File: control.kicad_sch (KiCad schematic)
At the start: 22 parts, among them Q1601 SI2369, Q1602 BSS138, Q1603 MMBT3904, Q1604 SI2369, Q1605 BSS138, Q1606 MMBT3904

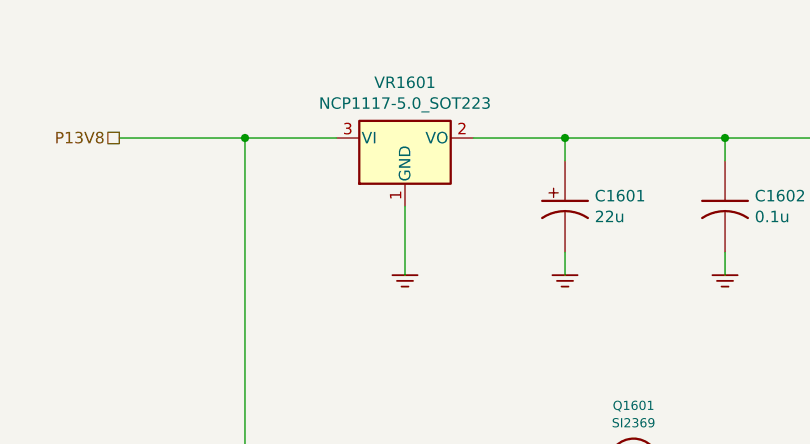
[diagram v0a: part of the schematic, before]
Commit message: Update pcb database to version 6
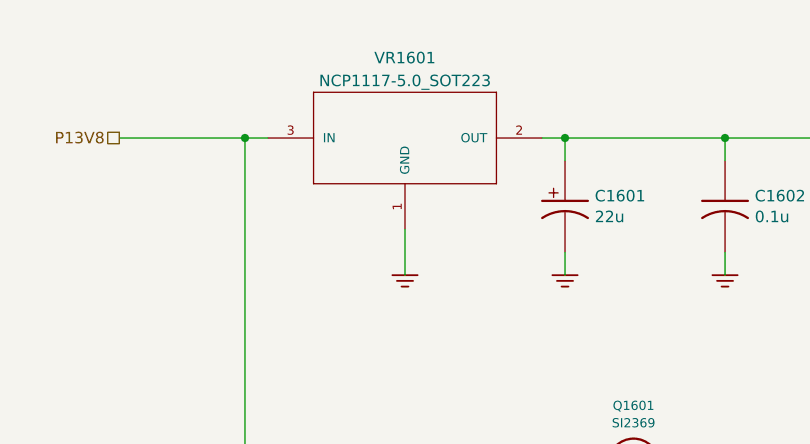
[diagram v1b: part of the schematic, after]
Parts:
- C1601: symbol Custom:CP_US -> custom:CP_US; PartNumber 800267-226 -> 80000X-XXX
- C1602: symbol Custom:C_US_0805_0.1UF_X7R_10%_50V_HS -> custom:C_US_0805_0.1UF_X7R_10%_50V_HS
- C1603: footprint Capacitor_SMD:C_0805_2012Metric_Pad1.15x1.40mm_HandSolder -> Capacitor_SMD:C_0603_1608Metric; symbol Custom:C_US -> custom:C_US; PartNumber 800003-475 -> 800063-XXX
- Q1601, Q1604: footprint mods:SOT23-3-SAR -> SOT-23; symbol Custom:AO3407 -> custom:AO3407
- Q1602, Q1605: footprint mods:SOT23-3-SAR -> SOT-23; symbol Custom:BSS138 -> custom:BSS138
- Q1603, Q1606: symbol Custom:MMBT3904 -> custom:MMBT3904
- R1601: symbol Custom:R_US_0805_1%_HS -> custom:R_US_0805_1%_HS; PartNumber 800235-471 -> 800235-XXX
- R1602, R1605, R1606, R1609: symbol Custom:R_US_0805_1%_HS -> custom:R_US_0805_1%_HS; PartNumber 800235-103 -> 800235-XXX
- R1603, R1607: symbol Custom:R_US_0805_1%_HS -> custom:R_US_0805_1%_HS; PartNumber 800235-100 -> 800235-XXX
- R1604, R1608: symbol Custom:R_US_0805_1%_HS -> custom:R_US_0805_1%_HS; PartNumber 800235-101 -> 800235-XXX
- TP1601, TP1602, TP1603: footprint mods:TESTPIN -> TESTPIN; symbol Custom:TESTPINTPSQ025 -> custom:TESTPINTPSQ025
- VR1601: footprint Package_TO_SOT_SMD:SOT-223-3_TabPin2 -> SOT223; symbol Regulator_Linear:NCP1117-5.0_SOT223 -> custom:NCP1117ST50

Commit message: Sync PCB with schematic
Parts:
- VR1601: footprint SOT223 -> Package_TO_SOT_SMD:SOT-223
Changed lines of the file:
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@@
     (property "Reference" "VR1601" (id 0) (at 64.77 29.21 0))
     (property "Value" "NCP1117-5.0_SOT223" (id 1) (at 64.77 31.75 0))
-    (property "Footprint" "SOT223" (id 2) (at 64.77 34.29 0)
+    (property "Footprint" "Package_TO_SOT_SMD:SOT-223" (id 2) (at 64.77 34.29 0)
       (effects (font (size 1.27 1.27)) hide)
     )

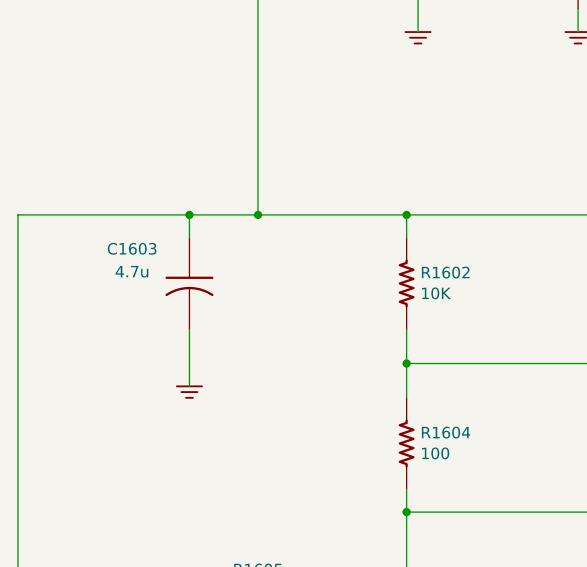
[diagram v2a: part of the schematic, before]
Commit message: Fix BOM part number errors and out of sync footprints which happened during conversion from Kicad 5 to 6
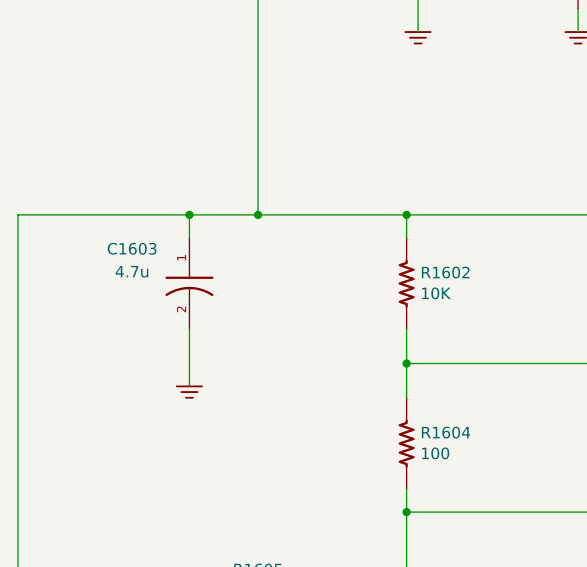
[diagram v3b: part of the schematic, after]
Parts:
- C1601: PartNumber 80000X-XXX -> 800267-226
- C1603: footprint Capacitor_SMD:C_0603_1608Metric -> Capacitor_SMD:C_0805_2012Metric_Pad1.18x1.45mm_HandSolder; PartNumber 800063-XXX -> 800003-475
- Q1602, Q1605: footprint SOT-23 -> mods:SOT23-3-SAR
- R1601: PartNumber 800235-XXX -> 800235-471
- R1602, R1605, R1606, R1609: PartNumber 800235-XXX -> 800235-103
- R1603, R1607: PartNumber 800235-XXX -> 800235-100
- R1604, R1608: PartNumber 800235-XXX -> 800235-101
- VR1601: footprint Package_TO_SOT_SMD:SOT-223 -> Package_TO_SOT_SMD:SOT-223-3_TabPin2
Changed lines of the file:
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@@
       (effects (font (size 1.524 1.524)))
     )
-    (property "PartNumber" "800235-XXX" (id 4) (at 68.072 78.74 90)
+    (property "PartNumber" "800235-103" (id 4) (at 68.072 78.74 90)
       (effects (font (size 1.524 1.524)) hide)
     )
@@
       (effects (font (size 1.524 1.524)))
     )
-    (property "PartNumber" "800235-XXX" (id 4) (at 68.072 96.52 90)
+    (property "PartNumber" "800235-101" (id 4) (at 68.072 96.52 90)
       (effects (font (size 1.524 1.524)) hide)
     )
@@
       (effects (font (size 1.524 1.524)))
     )
-    (property "PartNumber" "800235-XXX" (id 4) (at 49.53 122.682 90)
+    (property "PartNumber" "800235-103" (id 4) (at 49.53 122.682 90)
       (effects (font (size 1.524 1.524)) hide)
     )
@@
       (effects (font (size 1.524 1.524)))
     )
-    (property "PartNumber" "800235-XXX" (id 4) (at 113.792 81.28 90)
+    (property "PartNumber" "800235-100" (id 4) (at 113.792 81.28 90)
       (effects (font (size 1.524 1.524)) hide)
     )
@@
       (effects (font (size 1.016 1.016)) (justify left))
     )
-    (property "Footprint" "SOT-23" (id 2) (at 103.378 102.8192 0)
+    (property "Footprint" "mods:SOT23-3-SAR" (id 2) (at 103.378 102.8192 0)
       (effects (font (size 0.7366 0.7366)) hide)
     )
@@
       (effects (font (size 1.524 1.524)))
     )
-    (property "PartNumber" "800235-XXX" (id 4) (at 68.072 142.24 90)
+    (property "PartNumber" "800235-103" (id 4) (at 68.072 142.24 90)
       (effects (font (size 1.524 1.524)) hide)
     )
@@
       (effects (font (size 1.524 1.524)))
     )
-    (property "PartNumber" "800235-XXX" (id 4) (at 68.072 160.02 90)
+    (property "PartNumber" "800235-101" (id 4) (at 68.072 160.02 90)
       (effects (font (size 1.524 1.524)) hide)
     )
@@
       (effects (font (size 1.524 1.524)))
     )
-    (property "PartNumber" "800235-XXX" (id 4) (at 49.53 186.182 90)
+    (property "PartNumber" "800235-103" (id 4) (at 49.53 186.182 90)
       (effects (font (size 1.524 1.524)) hide)
     )
@@
       (effects (font (size 1.524 1.524)))
     )
-    (property "PartNumber" "800235-XXX" (id 4) (at 113.792 144.78 90)
+    (property "PartNumber" "800235-100" (id 4) (at 113.792 144.78 90)
       (effects (font (size 1.524 1.524)) hide)
     )
@@
       (effects (font (size 1.016 1.016)) (justify left))
     )
-    (property "Footprint" "SOT-23" (id 2) (at 103.378 166.3192 0)
+    (property "Footprint" "mods:SOT23-3-SAR" (id 2) (at 103.378 166.3192 0)
       (effects (font (size 0.7366 0.7366)) hide)
     )
@@
     (property "Reference" "C1603" (id 0) (at 33.02 77.47 0))
     (property "Value" "4.7u" (id 1) (at 33.02 80.01 0))
-    (property "Footprint" "Capacitor_SMD:C_0603_1608Metric" (id 2) (at 41.91 69.85 0)
+    (property "Footprint" "Capacitor_SMD:C_0805_2012Metric_Pad1.18x1.45mm_HandSolder" (id 2) (at 41.91 69.85 0)
       (effects (font (size 1.524 1.524)) hide)
     )
@@
       (effects (font (size 1.524 1.524)))
     )
-    (property "PartNumber" "800063-XXX" (id 4) (at 39.37 67.31 0)
+    (property "PartNumber" "800003-475" (id 4) (at 39.37 67.31 0)
       (effects (font (size 1.524 1.524)) hide)
     )
@@
     (property "Reference" "VR1601" (id 0) (at 64.77 29.21 0))
     (property "Value" "NCP1117-5.0_SOT223" (id 1) (at 64.77 31.75 0))
-    (property "Footprint" "Package_TO_SOT_SMD:SOT-223" (id 2) (at 64.77 34.29 0)
+    (property "Footprint" "Package_TO_SOT_SMD:SOT-223-3_TabPin2" (id 2) (at 64.77 34.29 0)
       (effects (font (size 1.27 1.27)) hide)
     )
@@
       (effects (font (size 1.524 1.524)))
     )
-    (property "PartNumber" "80000X-XXX" (id 4) (at 86.36 40.64 0)
+    (property "PartNumber" "800267-226" (id 4) (at 86.36 40.64 0)
       (effects (font (size 1.524 1.524)) hide)
     )
@@
       (effects (font (size 1.524 1.524)))
     )
-    (property "PartNumber" "800235-XXX" (id 4) (at 126.492 44.45 90)
-      (effects (font (size 1.524 1.524)) hide)
-    )
+    (property "PartNumber" "800235-471" (id 4) (at 126.492 44.45 90)
+      (effects (font (size 1.524 1.524)) hide)
+    )

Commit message: Change bias resistors on 2SC3357 amplifiers to stay under 12V across Vbe.
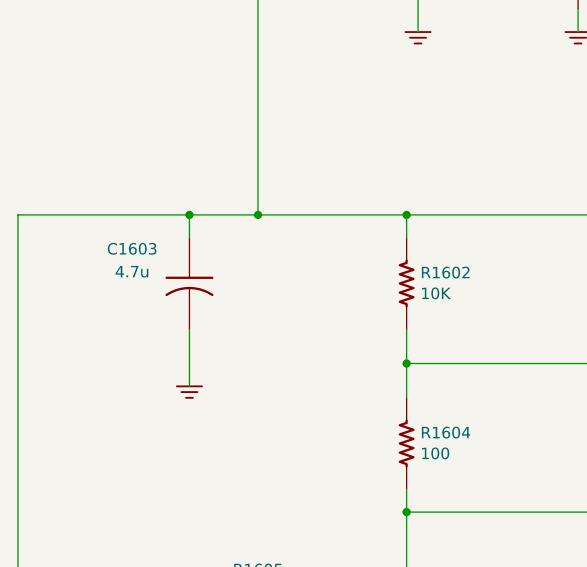
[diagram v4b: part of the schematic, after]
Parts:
- C1603: footprint Capacitor_SMD:C_0805_2012Metric_Pad1.18x1.45mm_HandSolder -> Capacitor_SMD:C_0603_1608Metric; PartNumber 800003-475 -> 800063-XXX
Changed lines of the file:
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@@
     (property "Reference" "C1603" (id 0) (at 33.02 77.47 0))
     (property "Value" "4.7u" (id 1) (at 33.02 80.01 0))
-    (property "Footprint" "Capacitor_SMD:C_0805_2012Metric_Pad1.18x1.45mm_HandSolder" (id 2) (at 41.91 69.85 0)
+    (property "Footprint" "Capacitor_SMD:C_0603_1608Metric" (id 2) (at 41.91 69.85 0)
       (effects (font (size 1.524 1.524)) hide)
     )
@@
       (effects (font (size 1.524 1.524)))
     )
-    (property "PartNumber" "800003-475" (id 4) (at 39.37 67.31 0)
+    (property "PartNumber" "800063-XXX" (id 4) (at 39.37 67.31 0)
       (effects (font (size 1.524 1.524)) hide)
     )

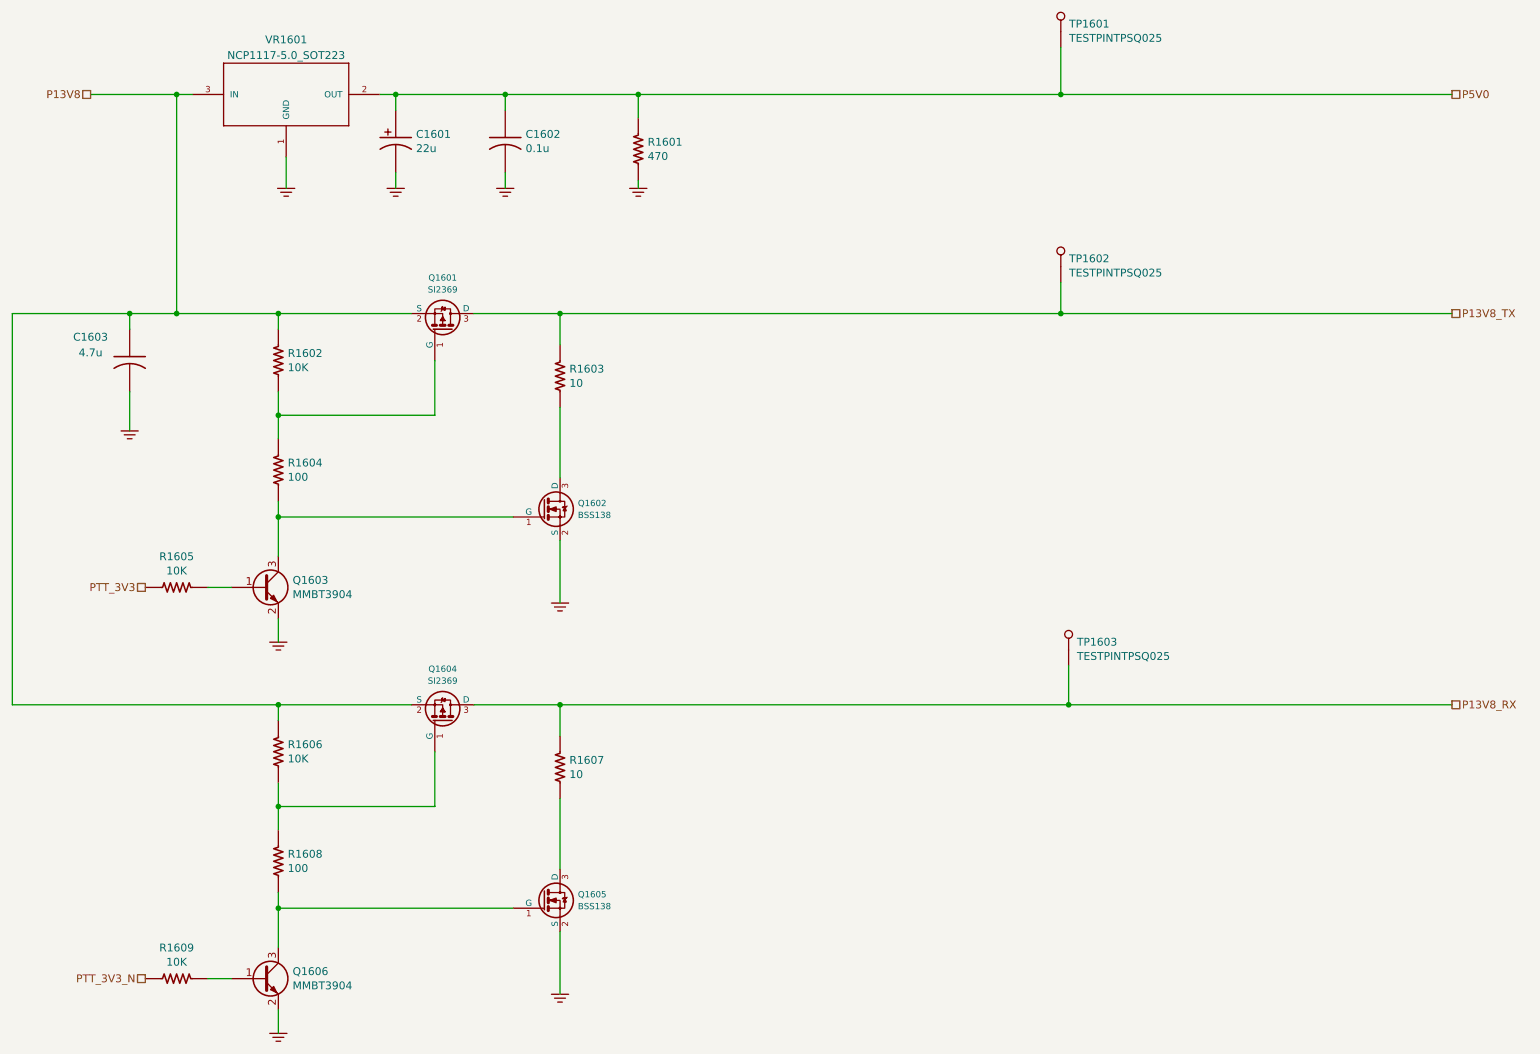
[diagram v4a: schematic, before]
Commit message: trx_mobo_concept_2_B. Change design to use a dedicated 8V supply for the 2SC3357 parts. Add S-Meter connector. Change mic connector to 3 pins and add 8V sopower supply to pin 3.
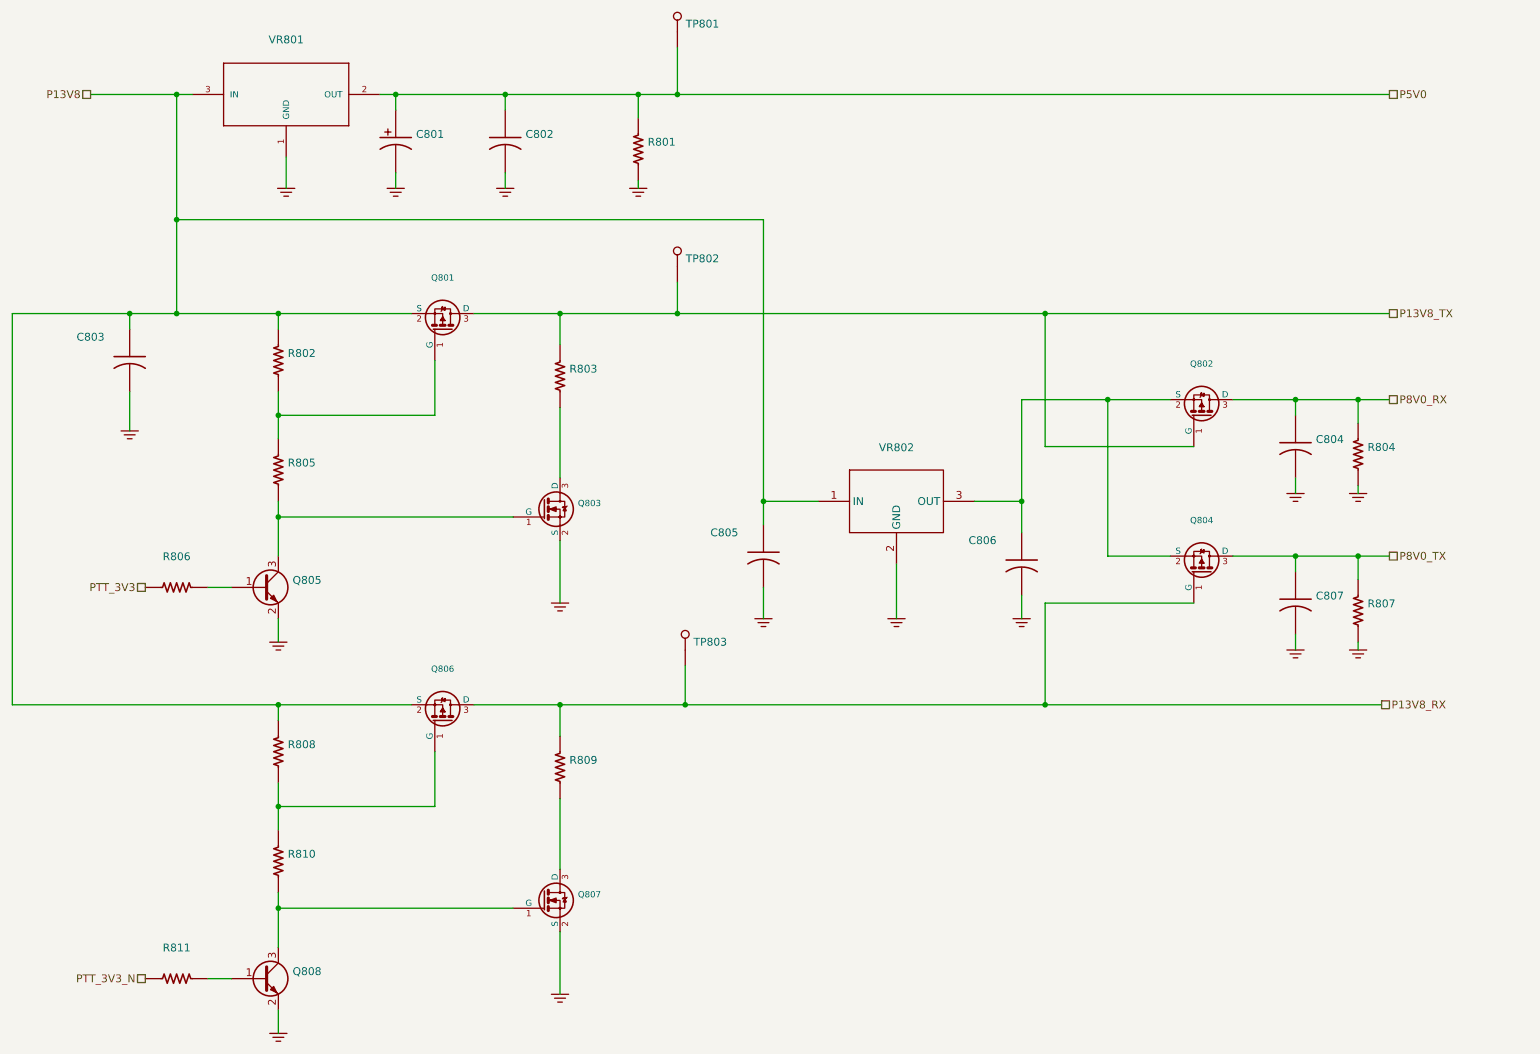
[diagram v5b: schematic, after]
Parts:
- added C804, C807: (no value), symbol custom:C_US_0805_0.1UF_X7R_10%_50V_HS
- added C805, C806: (no value), symbol custom:C_US
- added Q802, Q804: (no value), symbol custom:AO3407
- added R804, R807: (no value), symbol custom:R_US_0805_1%_HS
- added VR802: (no value), symbol custom:MC78M08CDTRKG
- C801: renamed from C1601; value 22u -> (none); footprint Capacitor_SMD:CP_Elec_6.3x5.7 -> (none)
- C802: renamed from C1602; value 0.1u -> (none); footprint Capacitor_SMD:C_0805_2012Metric_Pad1.15x1.40mm_HandSolder -> (none)
- C803: renamed from C1603; value 4.7u -> (none); footprint Capacitor_SMD:C_0603_1608Metric -> (none); PartNumber 800063-XXX -> 800003-475
- Q801: renamed from Q1601; value SI2369 -> (none); footprint SOT-23 -> (none)
- Q803: renamed from Q1602; value BSS138 -> (none); footprint mods:SOT23-3-SAR -> (none)
- Q805: renamed from Q1603; value MMBT3904 -> (none); footprint mods:SOT23-3-SAR -> (none)
- Q806: renamed from Q1604; value SI2369 -> (none); footprint SOT-23 -> (none)
- Q807: renamed from Q1605; value BSS138 -> (none); footprint mods:SOT23-3-SAR -> (none)
- Q808: renamed from Q1606; value MMBT3904 -> (none); footprint mods:SOT23-3-SAR -> (none)
- R801: renamed from R1601; value 470 -> (none); footprint Resistor_SMD:R_0805_2012Metric_Pad1.15x1.40mm_HandSolder -> (none)
- R802: renamed from R1602; value 10K -> (none); footprint Resistor_SMD:R_0805_2012Metric_Pad1.15x1.40mm_HandSolder -> (none)
- R803: renamed from R1603; value 10 -> (none); footprint Resistor_SMD:R_0805_2012Metric_Pad1.15x1.40mm_HandSolder -> (none)
- R805: renamed from R1604; value 100 -> (none); footprint Resistor_SMD:R_0805_2012Metric_Pad1.15x1.40mm_HandSolder -> (none)
- R806: renamed from R1605; value 10K -> (none); footprint Resistor_SMD:R_0805_2012Metric_Pad1.15x1.40mm_HandSolder -> (none)
- R808: renamed from R1606; value 10K -> (none); footprint Resistor_SMD:R_0805_2012Metric_Pad1.15x1.40mm_HandSolder -> (none)
- R809: renamed from R1607; value 10 -> (none); footprint Resistor_SMD:R_0805_2012Metric_Pad1.15x1.40mm_HandSolder -> (none)
- R810: renamed from R1608; value 100 -> (none); footprint Resistor_SMD:R_0805_2012Metric_Pad1.15x1.40mm_HandSolder -> (none)
- R811: renamed from R1609; value 10K -> (none); footprint Resistor_SMD:R_0805_2012Metric_Pad1.15x1.40mm_HandSolder -> (none)
- TP801: renamed from TP1601; value TESTPINTPSQ025 -> (none); footprint TESTPIN -> (none)
- TP802: renamed from TP1602; value TESTPINTPSQ025 -> (none); footprint TESTPIN -> (none)
- TP803: renamed from TP1603; value TESTPINTPSQ025 -> (none); footprint TESTPIN -> (none)
- VR801: renamed from VR1601; value NCP1117-5.0_SOT223 -> (none); footprint Package_TO_SOT_SMD:SOT-223-3_TabPin2 -> (none)
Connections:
- net GND: now also C804.2, C805.2, C806.2, C807.2, R804.2, R807.2, VR802.2 (GND)
- net P13V8: now also C805.1, VR802.1 (IN)
- net P13V8_RX: now also Q804.1 (G)
- net P13V8_TX: now also Q802.1 (G)
- new net: C806.1, Q802.2 (S), Q804.2 (S), VR802.3 (OUT)
- new net P8V0_RX: C804.1, Q802.3 (D), R804.1
- new net P8V0_TX: C807.1, Q804.3 (D), R807.1
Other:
- title: 5V LDO, 13.8V RX and TX Rails -> 5V LDO, 13.8V and 8.0V RX and TX Rails
- moved on the sheet: TP801, TP802, TP803
